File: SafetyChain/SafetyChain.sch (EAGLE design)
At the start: 5 parts, among them T1 BTA26-H

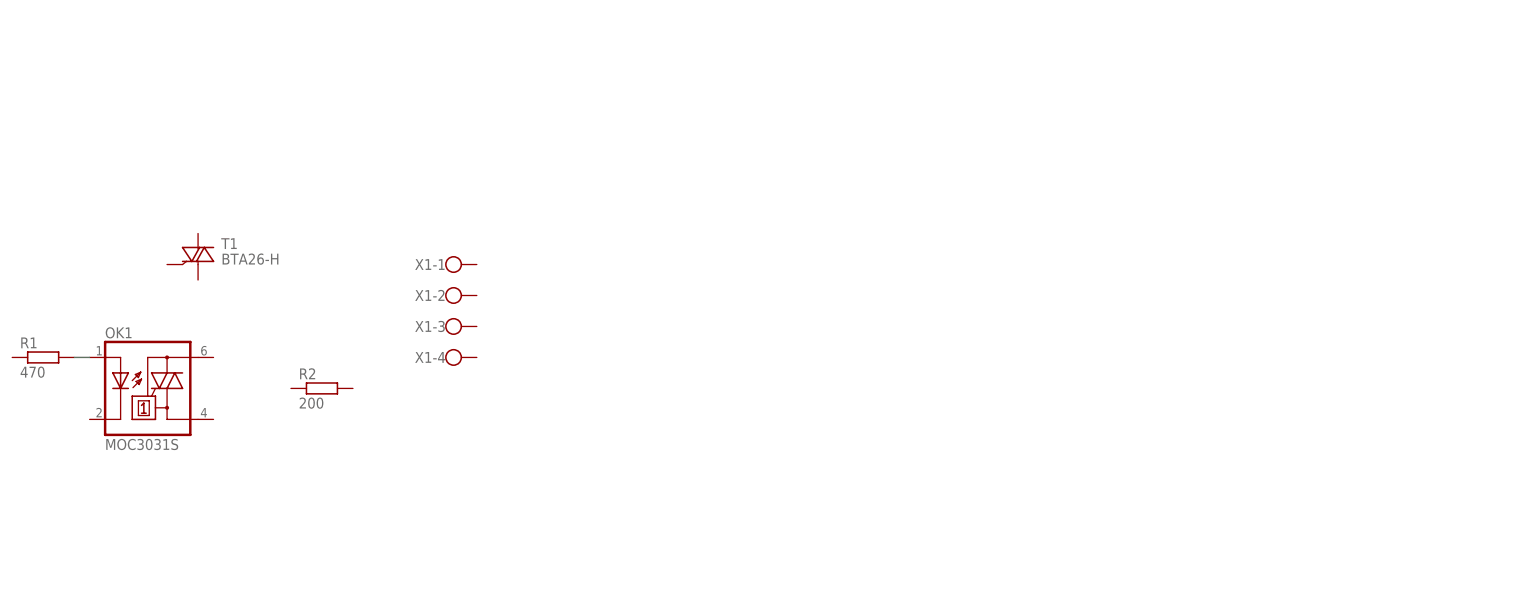
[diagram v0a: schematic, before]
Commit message: Re-routed a display pin to have the whole display on ports B and C. Safety chain board layouted.
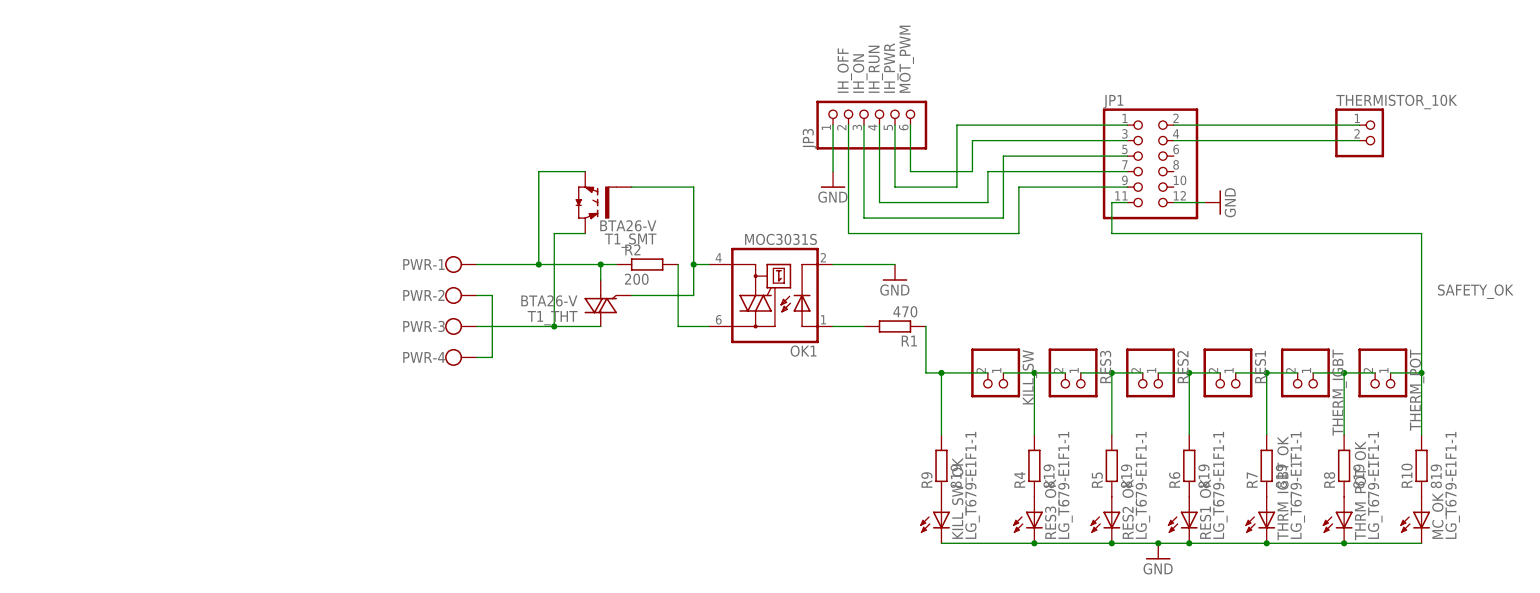
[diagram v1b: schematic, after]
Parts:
- removed T1: BTA26-H, triac:BTA26-H
- added JP1: (no value), pinhead:PINHD-2X6
- added JP3: (no value), pinhead:PINHD-1X6
- added KILL_SW, RES1, RES2, RES3, THERMISTOR_10K, THERM_IGBT, THERM_POT: (no value), pinhead:PINHD-1X2
- added KILL_SW_OK, MC_OK, RES1_OK, RES2_OK, RES3_OK, THRM_IGBT_OK, THRM_POT_OK: LG_T679-E1F1-1, led:LG_T679-E1F1-1
- added R10, R4, R5, R6, R7, R8, R9: 819, rcl:R-EU_M0805
- added T1_SMT: BTA26-V, transistor-power:IRG4BC15UD-S
- added T1_THT: BTA26-V, triac:BTA26-V
- renumbered X1 to PWR
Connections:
- new net 3V3: JP1.4, THERMISTOR_10K.2
- new net GND: JP1.12, JP3.1, KILL_SW_OK.C, MC_OK.C, OK1.C, RES1_OK.C, RES2_OK.C, RES3_OK.C, THRM_IGBT_OK.C, THRM_POT_OK.C
- new net IH_OFF: JP1.9, JP3.2
- new net IH_ON: JP1.5, JP3.3
- new net IH_PWR: JP1.1, JP3.5
- new net IH_RUN: JP1.7, JP3.4
- new net IH_THERMISTOR: JP1.2, THERMISTOR_10K.1
- new net L_IN: PWR-1.KL, R2.1, T1_SMT.E, T1_THT.A1
- new net L_OUT: PWR-3.KL, T1_SMT.C, T1_THT.A2
- new net MOT_PWM: JP1.3, JP3.6
- new net N$10: R5.1, RES2_OK.A
- new net N$11: R6.1, RES1_OK.A
- new net N$12: R7.1, THRM_IGBT_OK.A
- new net N$13: R8.1, THRM_POT_OK.A
- new net N$14: MC_OK.A, R10.1
- new net N$15: KILL_SW_OK.A, R9.1
- new net N$2: OK1.A2, R2.2
- new net N$3: R8.2, THERM_IGBT.1, THERM_POT.2
- new net N$4: R7.2, RES1.1, THERM_IGBT.2
- new net N$5: R6.2, RES1.2, RES2.1
- new net N$6: R5.2, RES2.2, RES3.1
- new net N$7: KILL_SW.1, R4.2, RES3.2
- new net N$8: KILL_SW.2, R1.1, R9.2
- new net N$9: R4.1, RES3_OK.A
- new net PWR_N: PWR-2.KL, PWR-4.KL
- new net SAFETY_OK: JP1.11, R10.2, THERM_POT.1
- new net TRIAC_DRV: OK1.A1, T1_SMT.G, T1_THT.G
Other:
- moved on the sheet: OK1, R1, R2

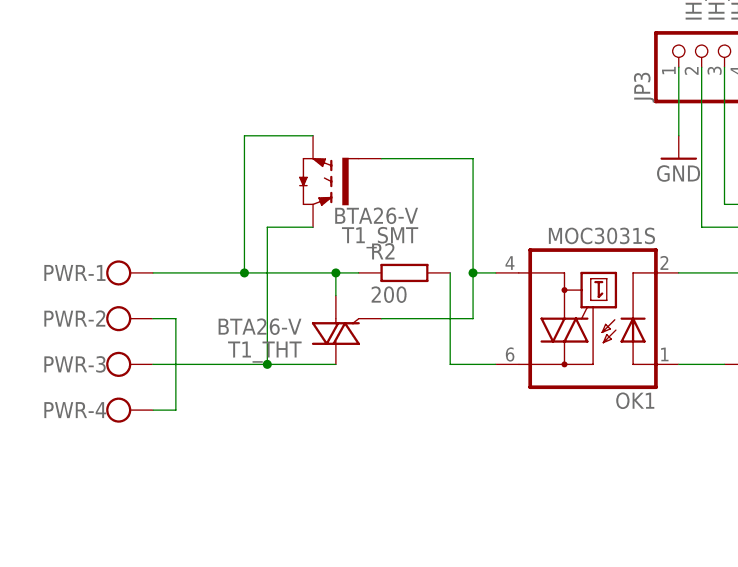
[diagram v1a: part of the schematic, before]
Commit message: Renamed files.
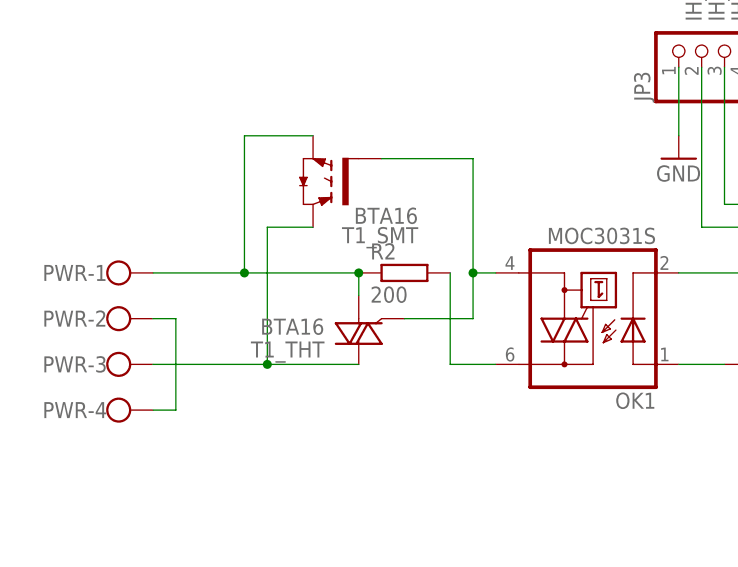
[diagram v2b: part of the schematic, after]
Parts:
- T1_SMT: value BTA26-V -> BTA16
- T1_THT: value BTA26-V -> BTA16; device triac:BTA26-V -> triac:BT138-V
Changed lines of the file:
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@@
 </classes>
 <parts>
-<part name="T1_THT" library="triac" deviceset="BTA26" device="-V" value="BTA26-V"/>
 <part name="OK1" library="optocoupler" deviceset="MOC30*" device="S" technology="31"/>
 <part name="R1" library="rcl" deviceset="R-EU_" device="M0805" value="470"/>
@@
 <part name="R10" library="rcl" deviceset="R-EU_" device="M0805" value="819"/>
 <part name="MC_OK" library="led" deviceset="*_T679-?-1" device="E1F1" technology="LG"/>
-<part name="T1_SMT" library="transistor-power" deviceset="IRG4BC15UD-" device="S" value="BTA26-V"/>
+<part name="T1_SMT" library="transistor-power" deviceset="IRG4BC15UD-" device="S" value="BTA16"/>
+<part name="T1_THT" library="triac" deviceset="BT138" device="-V" value="BTA16"/>
 </parts>
 <sheets>
@@
 </plain>
 <instances>
-<instance part="T1_THT" gate="-1" x="127" y="40.64" rot="R180"/>
 <instance part="OK1" gate="-1" x="154.94" y="40.64" rot="R180"/>
 <instance part="R1" gate="G$1" x="175.26" y="35.56" rot="R180"/>
@@
 <instance part="MC_OK" gate="G$1" x="261.62" y="5.08"/>
 <instance part="T1_SMT" gate="G$1" x="127" y="55.88" rot="R180"/>
+<instance part="T1_THT" gate="G$1" x="129.54" y="40.64" rot="R180"/>
 </instances>
 <busses>
@@
 <segment>
 <pinref part="PWR" gate="-1" pin="KL"/>
-<pinref part="T1_THT" gate="-1" pin="A1"/>
 <wire x1="106.68" y1="45.72" x2="116.84" y2="45.72" width="0.1524" layer="91"/>
-<wire x1="116.84" y1="45.72" x2="127" y2="45.72" width="0.1524" layer="91"/>
-<wire x1="127" y1="45.72" x2="127" y2="43.18" width="0.1524" layer="91"/>
-<wire x1="127" y1="45.72" x2="129.54" y2="45.72" width="0.1524" layer="91"/>
-<junction x="127" y="45.72"/>
+<wire x1="116.84" y1="45.72" x2="129.54" y2="45.72" width="0.1524" layer="91"/>
 <pinref part="R2" gate="G$1" pin="1"/>
 <pinref part="T1_SMT" gate="G$1" pin="E"/>
@@
 <wire x1="116.84" y1="60.96" x2="116.84" y2="45.72" width="0.1524" layer="91"/>
 <junction x="116.84" y="45.72"/>
+<pinref part="T1_THT" gate="G$1" pin="A1"/>
+<wire x1="129.54" y1="43.18" x2="129.54" y2="45.72" width="0.1524" layer="91"/>
+<junction x="129.54" y="45.72"/>
 </segment>
 </net>
 <net name="L_OUT" class="0">
 <segment>
-<pinref part="T1_THT" gate="-1" pin="A2"/>
 <pinref part="PWR" gate="-3" pin="KL"/>
-<wire x1="127" y1="35.56" x2="119.38" y2="35.56" width="0.1524" layer="91"/>
 <pinref part="T1_SMT" gate="G$1" pin="C"/>
 <wire x1="119.38" y1="35.56" x2="106.68" y2="35.56" width="0.1524" layer="91"/>
@@
 <wire x1="119.38" y1="50.8" x2="119.38" y2="35.56" width="0.1524" layer="91"/>
 <junction x="119.38" y="35.56"/>
+<pinref part="T1_THT" gate="G$1" pin="A2"/>
+<wire x1="129.54" y1="35.56" x2="119.38" y2="35.56" width="0.1524" layer="91"/>
 </segment>
 </net>
@@
 <wire x1="144.78" y1="45.72" x2="142.24" y2="45.72" width="0.1524" layer="91"/>
 <wire x1="142.24" y1="45.72" x2="142.24" y2="40.64" width="0.1524" layer="91"/>
-<pinref part="T1_THT" gate="-1" pin="G"/>
-<wire x1="142.24" y1="40.64" x2="132.08" y2="40.64" width="0.1524" layer="91"/>
+<wire x1="142.24" y1="40.64" x2="134.62" y2="40.64" width="0.1524" layer="91"/>
 <pinref part="T1_SMT" gate="G$1" pin="G"/>
 <wire x1="132.08" y1="58.42" x2="142.24" y2="58.42" width="0.1524" layer="91"/>
 <wire x1="142.24" y1="58.42" x2="142.24" y2="45.72" width="0.1524" layer="91"/>
 <junction x="142.24" y="45.72"/>
+<pinref part="T1_THT" gate="G$1" pin="G"/>
 </segment>
 </net>

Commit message: Redesign of all boards.
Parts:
- removed T1_SMT: BTA16, transistor-power:IRG4BC15UD-S
- added PWR_SW_LED: (no value), pinhead:PINHD-1X2
- R10, R4, R5, R6, R7, R8, R9: value 819 -> 1k
- T1_THT: USE_DEVICE (none) -> BTA_16
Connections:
- net GND: now also PWR_SW_LED.2
- net L_IN: no longer T1_SMT.E
- net L_OUT: no longer T1_SMT.C
- net N$8: now also PWR_SW_LED.1
- net TRIAC_DRV: no longer T1_SMT.G
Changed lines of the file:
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@@
 <grid distance="0.1" unitdist="inch" unit="inch" style="lines" multiple="1" display="no" altdistance="0.01" altunitdist="inch" altunit="inch"/>
 <layers>
-<layer number="1" name="Top" color="4" fill="1" visible="no" active="no"/>
-<layer number="16" name="Bottom" color="1" fill="1" visible="no" active="no"/>
-<layer number="17" name="Pads" color="2" fill="1" visible="no" active="no"/>
-<layer number="18" name="Vias" color="2" fill="1" visible="no" active="no"/>
-<layer number="19" name="Unrouted" color="6" fill="1" visible="no" active="no"/>
-<layer number="20" name="Dimension" color="15" fill="1" visible="no" active="no"/>
-<layer number="21" name="tPlace" color="7" fill="1" visible="no" active="no"/>
-<layer number="22" name="bPlace" color="7" fill="1" visible="no" active="no"/>
-<layer number="23" name="tOrigins" color="15" fill="1" visible="no" active="no"/>
-<layer number="24" name="bOrigins" color="15" fill="1" visible="no" active="no"/>
-<layer number="25" name="tNames" color="7" fill="1" visible="no" active="no"/>
-<layer number="26" name="bNames" color="7" fill="1" visible="no" active="no"/>
-<layer number="27" name="tValues" color="7" fill="1" visible="no" active="no"/>
-<layer number="28" name="bValues" color="7" fill="1" visible="no" active="no"/>
+<layer number="1" name="Top" color="4" fill="1" visible="yes" active="no"/>
+<layer number="16" name="Bottom" color="1" fill="1" visible="yes" active="no"/>
+<layer number="17" name="Pads" color="2" fill="1" visible="yes" active="no"/>
+<layer number="18" name="Vias" color="2" fill="1" visible="yes" active="no"/>
+<layer number="19" name="Unrouted" color="6" fill="1" visible="yes" active="no"/>
+<layer number="20" name="Dimension" color="15" fill="1" visible="yes" active="no"/>
+<layer number="21" name="tPlace" color="7" fill="1" visible="yes" active="no"/>
+<layer number="22" name="bPlace" color="7" fill="1" visible="yes" active="no"/>
+<layer number="23" name="tOrigins" color="15" fill="1" visible="yes" active="no"/>
+<layer number="24" name="bOrigins" color="15" fill="1" visible="yes" active="no"/>
+<layer number="25" name="tNames" color="7" fill="1" visible="yes" active="no"/>
+<layer number="26" name="bNames" color="7" fill="1" visible="yes" active="no"/>
+<layer number="27" name="tValues" color="7" fill="1" visible="yes" active="no"/>
+<layer number="28" name="bValues" color="7" fill="1" visible="yes" active="no"/>
 <layer number="29" name="tStop" color="7" fill="3" visible="no" active="no"/>
 <layer number="30" name="bStop" color="7" fill="6" visible="no" active="no"/>
@@
 <layer number="35" name="tGlue" color="7" fill="4" visible="no" active="no"/>
 <layer number="36" name="bGlue" color="7" fill="5" visible="no" active="no"/>
-<layer number="37" name="tTest" color="7" fill="1" visible="no" active="no"/>
-<layer number="38" name="bTest" color="7" fill="1" visible="no" active="no"/>
+<layer number="37" name="tTest" color="7" fill="1" visible="yes" active="no"/>
+<layer number="38" name="bTest" color="7" fill="1" visible="yes" active="no"/>
 <layer number="39" name="tKeepout" color="4" fill="11" visible="no" active="no"/>
 <layer number="40" name="bKeepout" color="1" fill="11" visible="no" active="no"/>
@@
 <layer number="44" name="Drills" color="7" fill="1" visible="no" active="no"/>
 <layer number="45" name="Holes" color="7" fill="1" visible="no" active="no"/>
-<layer number="46" name="Milling" color="3" fill="1" visible="no" active="no"/>
-<layer number="47" name="Measures" color="7" fill="1" visible="no" active="no"/>
-<layer number="48" name="Document" color="7" fill="1" visible="no" active="no"/>
-<layer number="49" name="Reference" color="7" fill="1" visible="no" active="no"/>
-<layer number="51" name="tDocu" color="7" fill="1" visible="no" active="no"/>
-<layer number="52" name="bDocu" color="7" fill="1" visible="no" active="no"/>
+<layer number="46" name="Milling" color="3" fill="1" visible="yes" active="no"/>
+<layer number="47" name="Measures" color="7" fill="1" visible="yes" active="no"/>
+<layer number="48" name="Document" color="7" fill="1" visible="yes" active="no"/>
+<layer number="49" name="Reference" color="7" fill="1" visible="yes" active="no"/>
+<layer number="51" name="tDocu" color="7" fill="1" visible="yes" active="no"/>
+<layer number="52" name="bDocu" color="7" fill="1" visible="yes" active="no"/>
 <layer number="91" name="Nets" color="2" fill="1" visible="yes" active="yes"/>
 <layer number="92" name="Busses" color="1" fill="1" visible="yes" active="yes"/>
@@
 <part name="RES3" library="pinhead" deviceset="PINHD-1X2" device=""/>
 <part name="KILL_SW" library="pinhead" deviceset="PINHD-1X2" device=""/>
-<part name="R4" library="rcl" deviceset="R-EU_" device="M0805" value="819"/>
-<part name="R5" library="rcl" deviceset="R-EU_" device="M0805" value="819"/>
-<part name="R6" library="rcl" deviceset="R-EU_" device="M0805" value="819"/>
-<part name="R7" library="rcl" deviceset="R-EU_" device="M0805" value="819"/>
-<part name="R8" library="rcl" deviceset="R-EU_" device="M0805" value="819"/>
+<part name="R4" library="rcl" deviceset="R-EU_" device="M0805" value="1k"/>
+<part name="R5" library="rcl" deviceset="R-EU_" device="M0805" value="1k"/>
+<part name="R6" library="rcl" deviceset="R-EU_" device="M0805" value="1k"/>
+<part name="R7" library="rcl" deviceset="R-EU_" device="M0805" value="1k"/>
+<part name="R8" library="rcl" deviceset="R-EU_" device="M0805" value="1k"/>
 <part name="RES2_OK" library="led" deviceset="*_T679-?-1" device="E1F1" technology="LG"/>
 <part name="RES1_OK" library="led" deviceset="*_T679-?-1" device="E1F1" technology="LG"/>
@@
 <part name="GND4" library="supply1" deviceset="GND" device=""/>
 <part name="KILL_SW_OK" library="led" deviceset="*_T679-?-1" device="E1F1" technology="LG"/>
-<part name="R9" library="rcl" deviceset="R-EU_" device="M0805" value="819"/>
-<part name="R10" library="rcl" deviceset="R-EU_" device="M0805" value="819"/>
+<part name="R9" library="rcl" deviceset="R-EU_" device="M0805" value="1k"/>
+<part name="R10" library="rcl" deviceset="R-EU_" device="M0805" value="1k"/>
 <part name="MC_OK" library="led" deviceset="*_T679-?-1" device="E1F1" technology="LG"/>
-<part name="T1_SMT" library="transistor-power" deviceset="IRG4BC15UD-" device="S" value="BTA16"/>
-<part name="T1_THT" library="triac" deviceset="BT138" device="-V" value="BTA16"/>
+<part name="T1_THT" library="triac" deviceset="BT138" device="-V" value="BTA16">
+<attribute name="USE_DEVICE" value="BTA_16"/>
+</part>
+<part name="PWR_SW_LED" library="pinhead" deviceset="PINHD-1X2" device=""/>
+<part name="GND5" library="supply1" deviceset="GND" device=""/>
 </parts>
 <sheets>
@@
 <instance part="R10" gate="G$1" x="261.62" y="12.7" rot="R90"/>
 <instance part="MC_OK" gate="G$1" x="261.62" y="5.08"/>
-<instance part="T1_SMT" gate="G$1" x="127" y="55.88" rot="R180"/>
-<instance part="T1_THT" gate="G$1" x="129.54" y="40.64" rot="R180"/>
+<instance part="T1_THT" gate="G$1" x="129.54" y="40.64" smashed="yes" rot="R180">
+<attribute name="USE_DEVICE" x="139.7" y="33.02" size="1.778" layer="96" rot="R180" display="both"/>
+<attribute name="NAME" x="125.73" y="38.1" size="1.778" layer="95" rot="R180"/>
+<attribute name="VALUE" x="128.27" y="43.18" size="1.778" layer="96" rot="R180"/>
+</instance>
+<instance part="PWR_SW_LED" gate="G$1" x="170.18" y="22.86" rot="R270"/>
+<instance part="GND5" gate="1" x="165.1" y="12.7"/>
 </instances>
 <busses>
@@
 <segment>
 <pinref part="PWR" gate="-1" pin="KL"/>
-<wire x1="106.68" y1="45.72" x2="116.84" y2="45.72" width="0.1524" layer="91"/>
-<wire x1="116.84" y1="45.72" x2="129.54" y2="45.72" width="0.1524" layer="91"/>
+<wire x1="106.68" y1="45.72" x2="129.54" y2="45.72" width="0.1524" layer="91"/>
 <pinref part="R2" gate="G$1" pin="1"/>
-<pinref part="T1_SMT" gate="G$1" pin="E"/>
-<wire x1="124.46" y1="60.96" x2="116.84" y2="60.96" width="0.1524" layer="91"/>
-<wire x1="116.84" y1="60.96" x2="116.84" y2="45.72" width="0.1524" layer="91"/>
-<junction x="116.84" y="45.72"/>
 <pinref part="T1_THT" gate="G$1" pin="A1"/>
 <wire x1="129.54" y1="43.18" x2="129.54" y2="45.72" width="0.1524" layer="91"/>
@@
 <segment>
 <pinref part="PWR" gate="-3" pin="KL"/>
-<pinref part="T1_SMT" gate="G$1" pin="C"/>
-<wire x1="119.38" y1="35.56" x2="106.68" y2="35.56" width="0.1524" layer="91"/>
-<wire x1="124.46" y1="50.8" x2="119.38" y2="50.8" width="0.1524" layer="91"/>
-<wire x1="119.38" y1="50.8" x2="119.38" y2="35.56" width="0.1524" layer="91"/>
-<junction x="119.38" y="35.56"/>
+<wire x1="129.54" y1="35.56" x2="106.68" y2="35.56" width="0.1524" layer="91"/>
 <pinref part="T1_THT" gate="G$1" pin="A2"/>
-<wire x1="129.54" y1="35.56" x2="119.38" y2="35.56" width="0.1524" layer="91"/>
 </segment>
 </net>
@@
 <wire x1="142.24" y1="45.72" x2="142.24" y2="40.64" width="0.1524" layer="91"/>
 <wire x1="142.24" y1="40.64" x2="134.62" y2="40.64" width="0.1524" layer="91"/>
-<pinref part="T1_SMT" gate="G$1" pin="G"/>
-<wire x1="132.08" y1="58.42" x2="142.24" y2="58.42" width="0.1524" layer="91"/>
-<wire x1="142.24" y1="58.42" x2="142.24" y2="45.72" width="0.1524" layer="91"/>
-<junction x="142.24" y="45.72"/>
 <pinref part="T1_THT" gate="G$1" pin="G"/>
 </segment>
@@
 <junction x="248.92" y="0"/>
 </segment>
+<segment>
+<pinref part="PWR_SW_LED" gate="G$1" pin="2"/>
+<wire x1="170.18" y1="25.4" x2="165.1" y2="25.4" width="0.1524" layer="91"/>
+<wire x1="165.1" y1="25.4" x2="165.1" y2="15.24" width="0.1524" layer="91"/>
+<pinref part="GND5" gate="1" pin="GND"/>
+</segment>
 </net>
 <net name="IH_OFF" class="0">
@@
 <wire x1="182.88" y1="17.78" x2="182.88" y2="27.94" width="0.1524" layer="91"/>
 <junction x="182.88" y="27.94"/>
-</segment>
-</net>
+<pinref part="PWR_SW_LED" gate="G$1" pin="1"/>
+<wire x1="180.34" y1="27.94" x2="172.72" y2="27.94" width="0.1524" layer="91"/>
+<wire x1="172.72" y1="27.94" x2="172.72" y2="25.4" width="0.1524" layer="91"/>
+<junction x="180.34" y="27.94"/>
+</segment>
+</net>
